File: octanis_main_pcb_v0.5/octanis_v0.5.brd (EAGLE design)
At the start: 69.2 x 41.9 mm, 78 parts, among them IC1 BME280, Q1 32.768kHz, Q2 32.768kHz, U3 DRV8836DSSR, U4 DRV8836DSSR, U5 DRV8836DSSR, U7 DRV8836DSSR

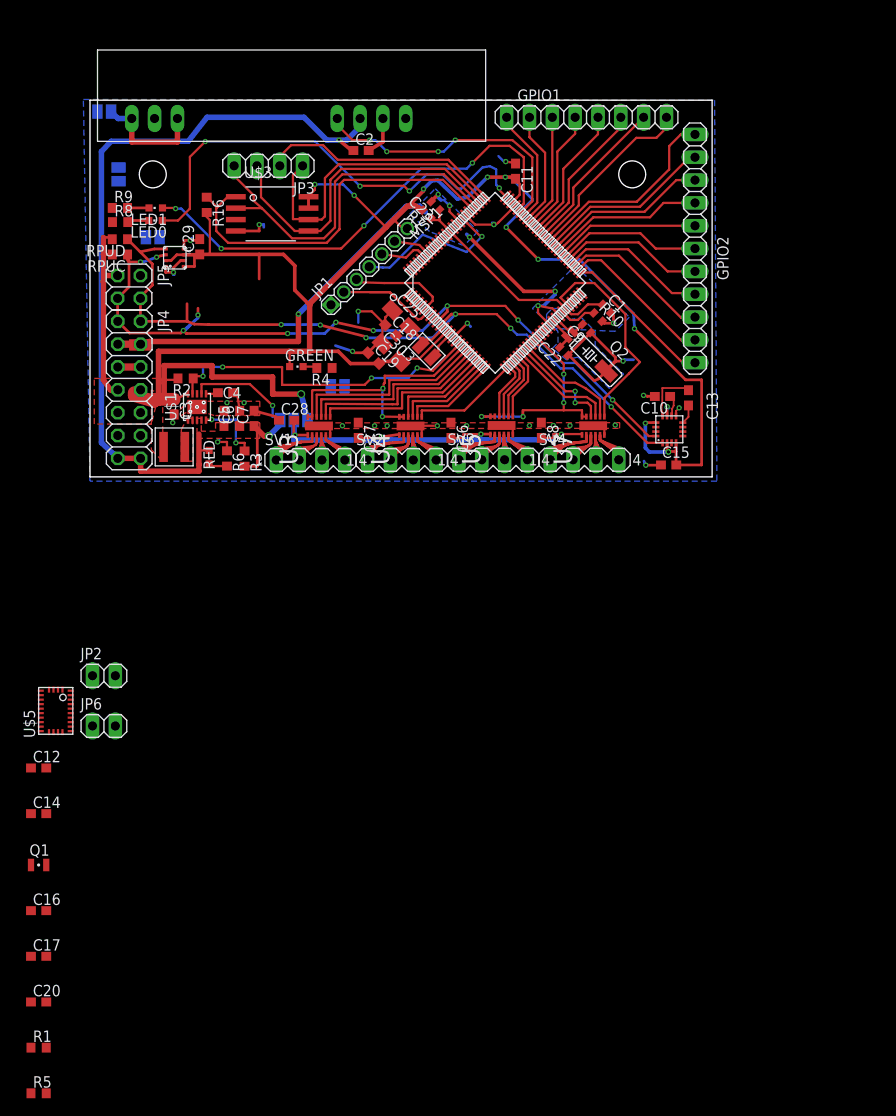
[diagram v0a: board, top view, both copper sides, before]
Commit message: rearranged GPIOs
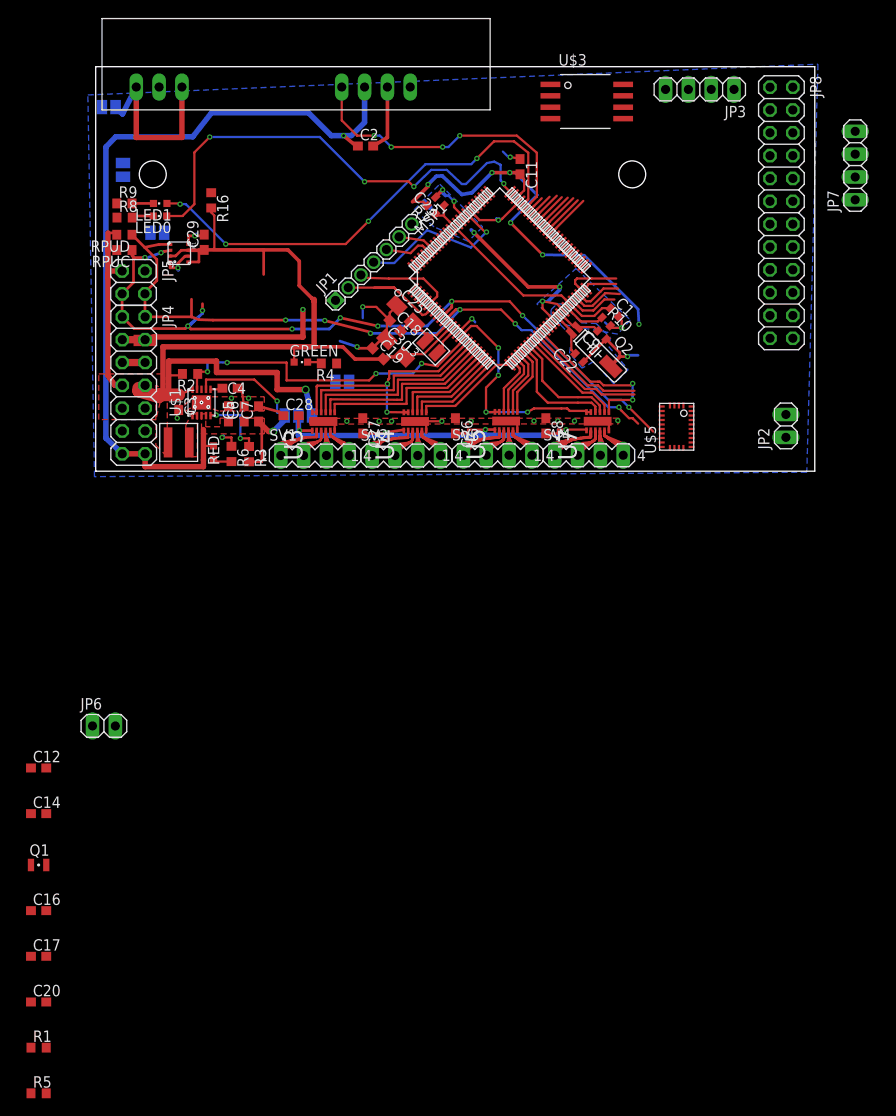
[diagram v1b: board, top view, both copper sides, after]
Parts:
- removed C10: 4.7u, rcl:C0603
- removed C13: 220n, rcl:C0603
- removed C15: 100n, rcl:C0603
- removed COMPASS: HMC5883L, HMC5883L:LPCC16
- removed GPIO1: A7:A0, pinhead:1X08
- removed GPIO2: A18:A8, pinhead:1X11
- added JP7: SPI, pinhead:1X04
- added JP8: (no value), pinhead:2X12
- moved JP2 80.8 mm to (76.8, 5.03), turned to 90 degrees
- moved U$5 76.0 mm to (64.6, 4.95)
- moved JP3 48.7 mm to (67.2, 42.5)
- moved U$3 37.2 mm to (53.5, 41.1)
- moved U$4 3.54 mm to (18.5, 42.7)
- moved C22 1.86 mm to (53.8, 12.6)
- moved C9 1.86 mm to (56.3, 15.2)
- moved R10 1.04 mm to (56.8, 16.6)
- moved C1 0.97 mm to (57.7, 17.7)
- moved C18 0.71 mm to (33.3, 16.2)
- moved C11 0.71 mm to (47.2, 33.9)
- moved C19 0.71 mm to (31.4, 13.1)
- moved C2 0.71 mm to (30.0, 36.2)
- moved C23 0.71 mm to (38.3, 30.0)
- moved C25 0.71 mm to (34.5, 17.4)
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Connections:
- removed net N$14: GPIO2.1, MSP1.61
- removed net N$15: GPIO2.2, MSP1.60
- removed net N$17: C10.1, COMPASS.10
- removed net N$20: GPIO2.3, MSP1.59
- removed net N$21: GPIO2.4, MSP1.58
- removed net N$22: GPIO2.5, MSP1.57
- removed net N$23: GPIO2.6, MSP1.56
- removed net N$25: C13.2, COMPASS.8
- removed net N$27: GPIO1.1, MSP1.69
- removed net N$28: GPIO1.2, MSP1.68
- removed net N$30: GPIO1.3, MSP1.67
- removed net N$32: C13.1, COMPASS.12
- removed net N$35: GPIO1.4, MSP1.66
- removed net N$36: GPIO1.5, MSP1.65
- removed net N$37: GPIO1.6, MSP1.64
- removed net N$38: GPIO1.8, MSP1.62
- removed net N$43: GPIO1.7, MSP1.63
- removed net P2.0/PM_UCA1STE: MSP1.16
- new net A0: JP8.1, MSP1.69
- new net A1: JP8.2, MSP1.68
- new net A10: JP8.11, MSP1.59
- new net A11: JP8.12, MSP1.58
- new net A12: JP8.13, MSP1.57
- new net A13: JP8.14, MSP1.56
- new net A2: JP8.3, MSP1.67
- new net A23: JP8.24, MSP1.46
- new net A3: JP8.4, MSP1.66
- new net A4: JP8.5, MSP1.65
- new net A5: JP8.6, MSP1.64
- new net A6: JP8.7, MSP1.63
- new net A7: JP8.8, MSP1.62
- new net A8: JP8.9, MSP1.61
- new net A9: JP8.10, MSP1.60
- net +3V3: no longer C15.2, COMPASS.13, COMPASS.2, COMPASS.4
- net A14: now also JP8.15; no longer GPIO2.7
- net A15: now also JP8.16; no longer GPIO2.8
- net A16: now also JP8.17; no longer GPIO2.9
- net A17: now also JP8.18; no longer GPIO2.10
- net A18: now also JP8.19; no longer GPIO2.11
- net A19: now also JP8.20
- net A20: now also JP8.21
- net A21: now also JP8.22
- net A22: now also JP8.23
- net GND: no longer C10.2, C15.1, COMPASS.11, COMPASS.9
- net M5678SLEEP: now also MSP1.16; no longer MSP1.36
- net M7IN1: now also MSP1.31; no longer MSP1.32
- net M7IN2: now also MSP1.32; no longer MSP1.31
- net M8IN2: now also MSP1.36; no longer MSP1.46
- net SCL: no longer COMPASS.1
- net SDA: no longer COMPASS.16
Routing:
- net +3V3: track 255.1 -> 188.5 mm, vias 12 -> 7
- net SPI_FLASH_CS: track 43.1 -> 0.00 mm
- net SPI_MISO: track 41.4 -> 0.00 mm
- net SPI_MOSI: track 36.5 -> 0.00 mm
- net SPI_SCK: track 34.1 -> 0.00 mm
- net SPI_EXTSLAVE_TE: track 26.7 -> 0.00 mm
- net N$14: track 22.6 -> 0.00 mm
- net N$38: track 20.2 -> 0.00 mm
- net N$15: track 19.8 -> 0.00 mm
- net N$20: track 18.5 -> 0.00 mm
- net N$43: track 17.6 -> 0.00 mm
- net N$21: track 17.3 -> 0.00 mm
- net A17: track 17.1 -> 0.00 mm
- net A18: track 16.8 -> 0.00 mm
- net A16: track 16.7 -> 0.00 mm
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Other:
- board size 69.2 x 41.9 mm -> 80 x 45 mm

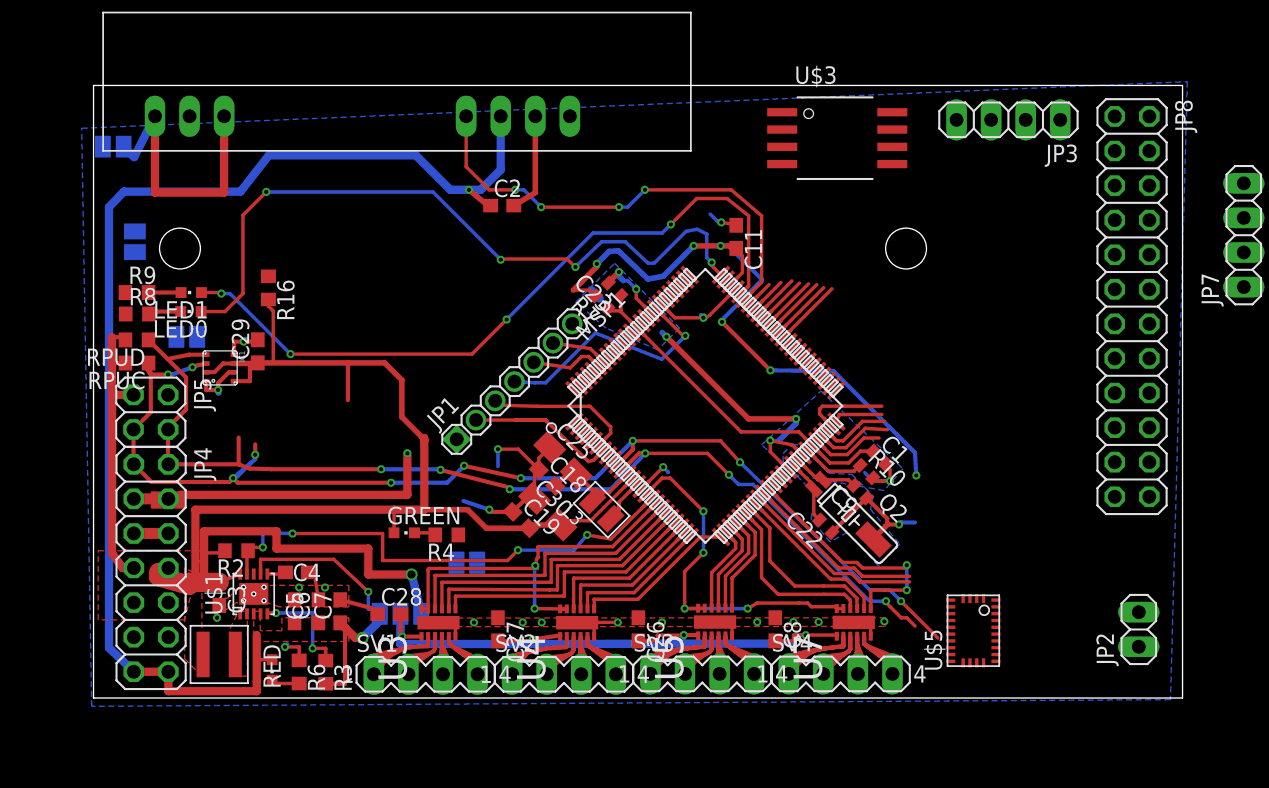
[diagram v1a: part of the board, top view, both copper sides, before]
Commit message: separated motor supply. added pull ups for sleep pin
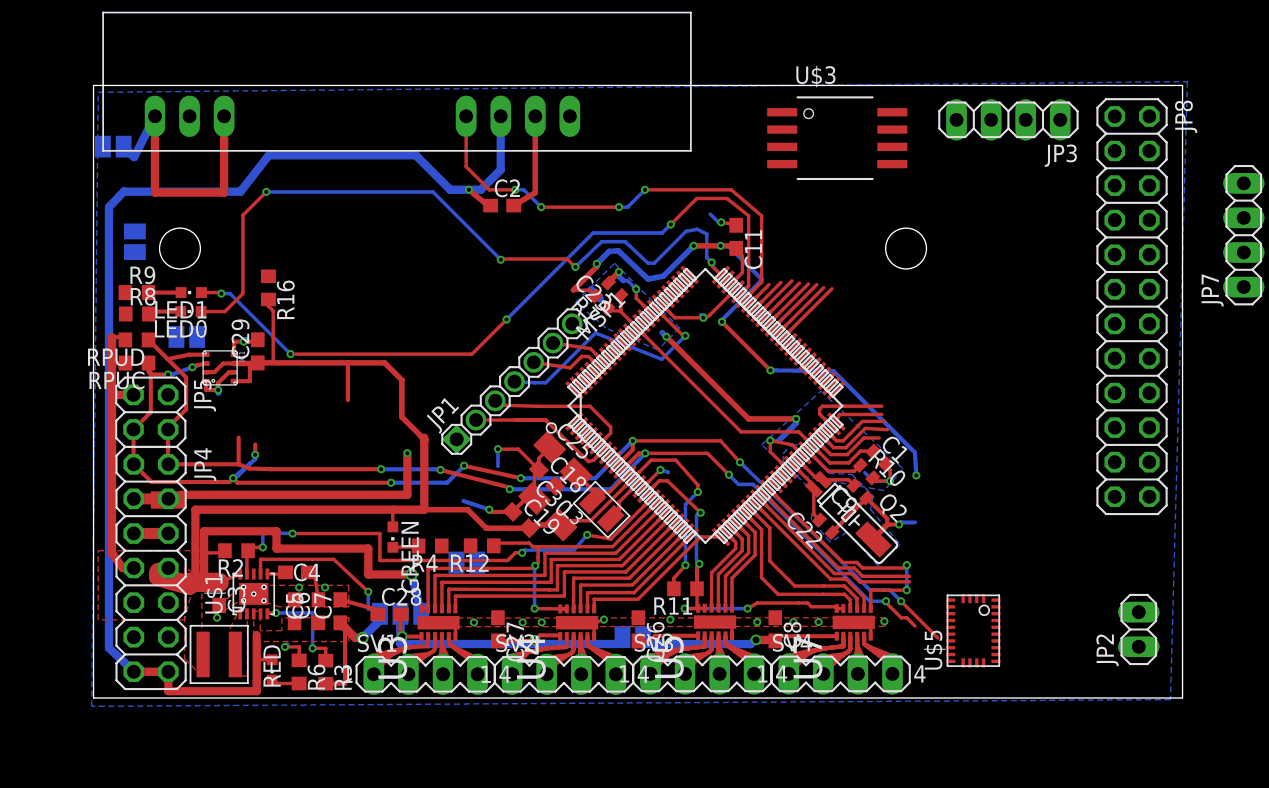
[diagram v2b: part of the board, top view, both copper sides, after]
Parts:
- added R11, R12: 10k, rcl:R0603
- added SJ6: (no value), jumper:SJ
- moved R4 1.47 mm to (24.7, 11.2)
- moved GREEN 0.90 mm to (22.0, 11.8), turned to 180 degrees
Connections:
- new net V_MOTOR2: C26.2, C8.2, SJ6.1, U5.1, U7.1
- net +3V3: now also R11.2, R12.2
- net M1234SLEEP: now also R12.1
- net M5678SLEEP: now also R11.1
- net V_MOTOR: now also SJ6.2; no longer C26.2, C8.2, U5.1, U7.1
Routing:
- net V_MOTOR: track 54.4 -> 30.7 mm, vias 4 -> 2
- net V_MOTOR2: track 0.00 -> 21.3 mm, vias 0 -> 2
- net +3V3: track 188.5 -> 202.7 mm, vias 7 -> 9
- net M1234SLEEP: track 28.6 -> 31.8 mm
- net GND: track 77.4 -> 76.2 mm
- net M5678SLEEP: track 26.8 -> 26.1 mm
- net N$4: track 1.59 -> 2.21 mm

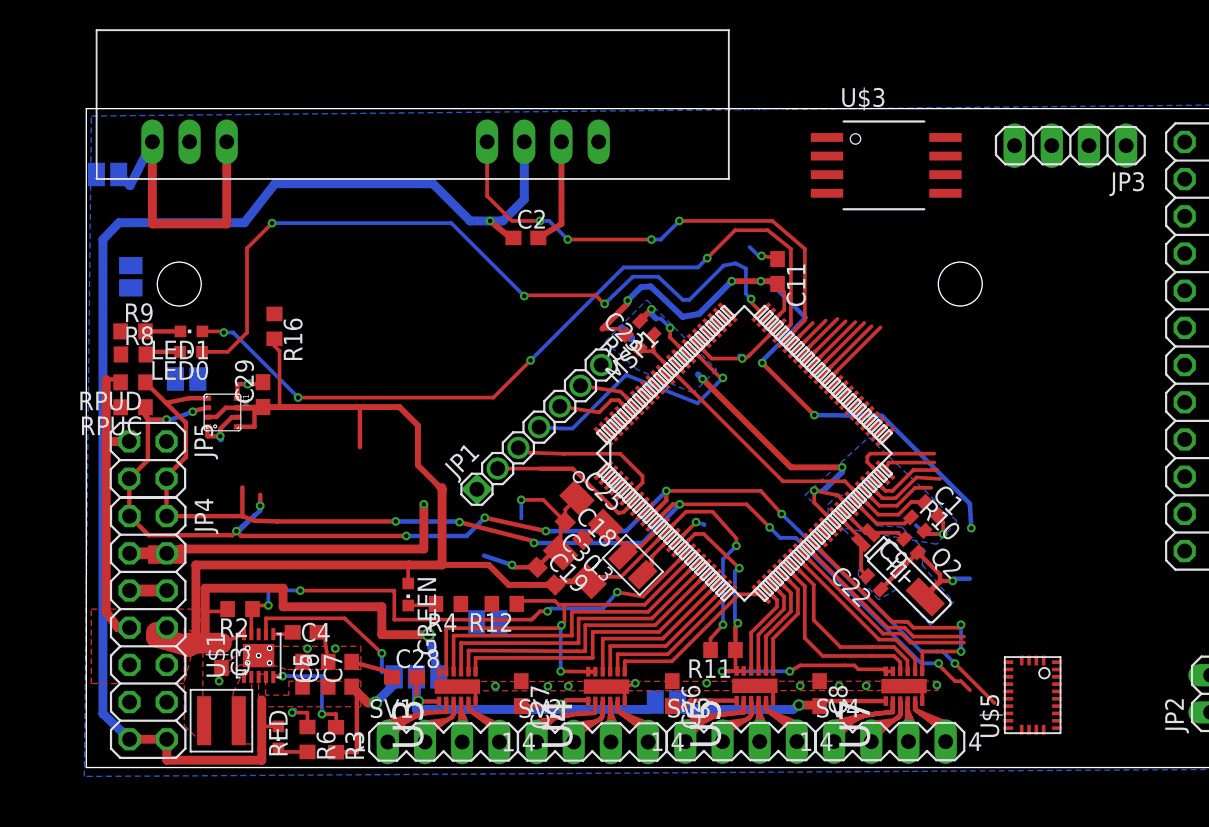
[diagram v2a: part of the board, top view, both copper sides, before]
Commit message: redesigned hx1 pins
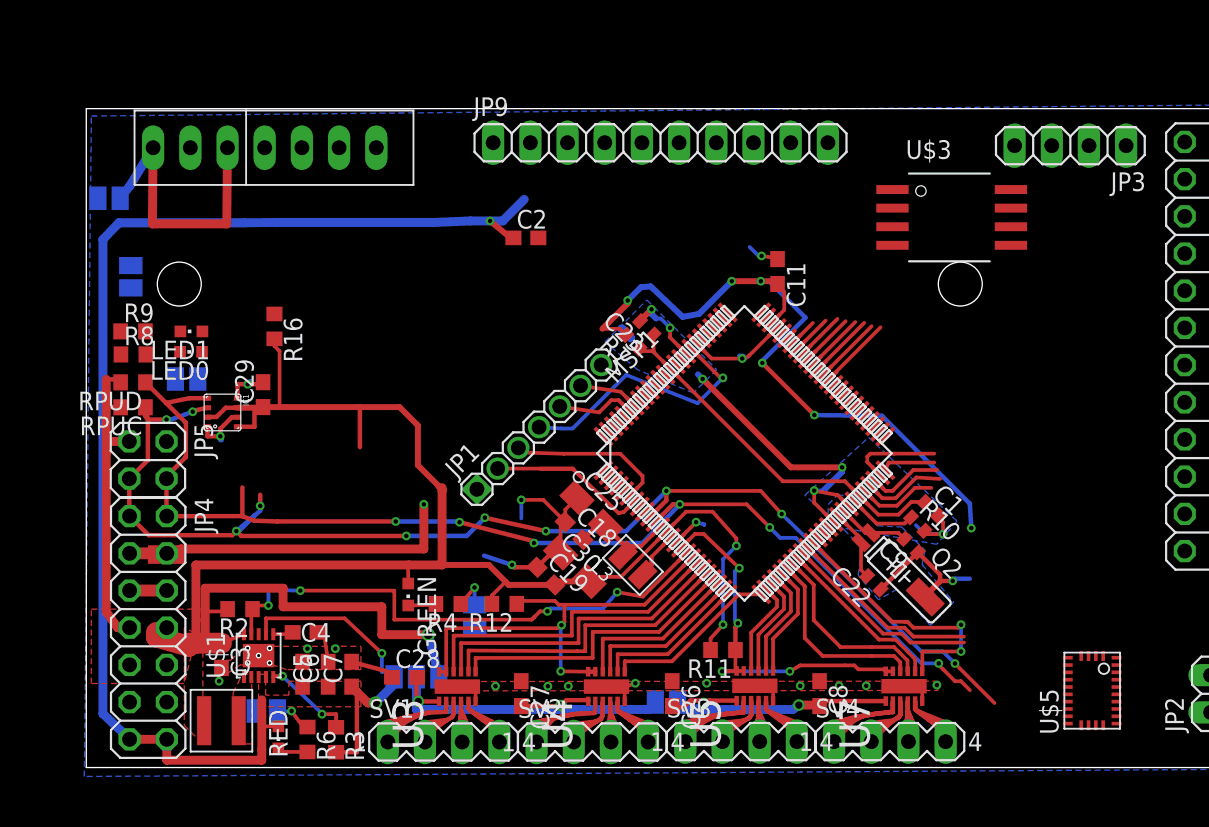
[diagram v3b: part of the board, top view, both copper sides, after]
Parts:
- added JP9: (no value), pinhead:1X10
- added SJ7: (no value), jumper:SJ
- U$4: value HX1 -> HX1EXTERNALMOUNT; device Octanis1:HX1 -> Octanis1:HX1_EXT
- moved U$4 13.9 mm to (4.56, 42.3)
- moved U$3 5.71 mm to (58.0, 37.6)
- moved U$5 4.08 mm to (68.7, 5.25)
- moved SJ2 1.63 mm to (1.55, 38.9)
- moved SJ3 0.99 mm to (26.5, 10.4), turned to 90 degrees
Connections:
- removed net P7.0/PM_SMCLK/PM_DMAE0: MSP1.88
- removed net P7.1/PM_C0OUT/PM_TA0CLK: MSP1.89
- removed net P7.2/PM_C1OUT/PM_TA1CLK: MSP1.90
- removed net P7.3/PM_TA0.0: MSP1.91
- new net N$14: R6.1, SJ7.2
- new net N$15: JP9.10, MSP1.88
- new net N$17: JP9.9, MSP1.89
- new net N$20: JP9.8, MSP1.90
- new net N$21: JP9.7, MSP1.91
- net GND: now also SJ7.1; no longer R6.1
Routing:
- net LED1: track 53.3 -> 0.00 mm, vias 4 -> 0
- net LED0: track 52.3 -> 0.00 mm, vias 4 -> 0
- net HX1_EN: track 34.5 -> 0.00 mm, vias 4 -> 0
- net GND: track 76.2 -> 66.4 mm, vias 21 -> 20
- net +5V: track 113.3 -> 107.0 mm
- net N$14: track 0.00 -> 2.83 mm, vias 0 -> 1
- net N$26: track 0.00 -> 2.64 mm, vias 0 -> 1
- net N$5: track 2.41 -> 0.00 mm
- net N$6: track 2.39 -> 0.00 mm
- net +3V3: track 202.7 -> 204.6 mm
- net N$2: track 7.81 -> 6.28 mm
- net RFGND: track 20.8 -> 19.6 mm

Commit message: assigned all GPIO
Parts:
- removed JP2: (no value), pinhead:1X02
- removed SJ4, SJ5: (no value), jumper:SJ
- added C10: 10u, rcl:A/3216-18R
- added JP10: (no value), pinhead:2X10
- JP3: value SPI -> (none); device pinhead:1X04 -> pinhead:2X02
- JP6: device pinhead:1X02 -> pinhead:2X02
- JP9: device pinhead:1X10 -> pinhead:2X02
- moved R5 114.1 mm to (76.2, 9.53)
- moved R1 107.3 mm to (69.8, 11.4), turned to 270 degrees
- moved C20 104.1 mm to (76.2, 4.45)
- moved C16 96.4 mm to (75.6, 1.91)
- moved C14 94.1 mm to (76.2, 6.99)
- moved C17 93.0 mm to (67.9, 1.91), turned to 180 degrees
- moved Q1 90.8 mm to (71.8, 2.54)
- moved C12 90.4 mm to (72.4, 11.4), turned to 270 degrees
- moved JP6 73.4 mm to (64.1, 8.89), turned to 90 degrees
- moved JP3 64.2 mm to (3.81, 32.4), turned to 90 degrees
- moved R16 54.5 mm to (66.2, 41.6), turned to 90 degrees
- moved SJ2 34.0 mm to (1.28, 4.87), turned to 90 degrees
- moved C2 17.4 mm to (12.8, 38.0)
- moved LED0 15.9 mm to (22.6, 32.3)
- moved R8 15.5 mm to (18.2, 32.2)
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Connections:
- removed net N$24: U$4.TXD
- removed net N$29: R8.1, SJ4.2
- removed net N$31: R9.1, SJ5.2
- removed net P1.0/UCA0STE: MSP1.4
- removed net P1.1/UCA0CLK: MSP1.5
- removed net P1.4/UCB0STE: MSP1.8
- removed net P1.5/UCB0CLK: MSP1.9
- removed net P10.0/UCB3STE: MSP1.100
- removed net P10.1/UCB3CLK: MSP1.1
- removed net P10.2/UCB3SIMO/UCB3SDA: MSP1.2
- removed net P10.3UCB3SOMI/UCB3SCL: MSP1.3
- removed net P3.5/PM_UCB2CLK: MSP1.37
- removed net P6.7/TA2.4/UCB3SOMI/UCB3SCL/C1.0: MSP1.81
- removed net P9.2/TA3.3: MSP1.74
- removed net P9.4/UCA3STE: MSP1.96
- removed net P9.5/UCA3CLK: MSP1.97
- removed net PJ.2/HFXOUT: MSP1.85
- removed net PJ.3/HFXIN: MSP1.86
- removed net PJ.4/TDI/ADC14CLK: MSP1.92
- removed net PJ.5/TDO/SWO: MSP1.93
- new net HX1_DATA: MSP1.8, U$4.TXD
- new net P1.0: JP10.20, MSP1.4
- new net P1.1: JP10.19, MSP1.5
- new net P10.2: JP10.17, MSP1.2
- new net P10.3: JP10.18, MSP1.3
- new net P5.6: JP10.7, MSP1.70
- new net P5.7: JP10.5, MSP1.71
- new net P6.6: JP10.10, MSP1.80
- new net P6.7: JP10.9, MSP1.81
- new net P9.2: JP10.3, MSP1.74
- new net P9.3: JP10.1, MSP1.75
- new net P9.4: JP10.15, MSP1.96
- new net P9.5: JP10.16, MSP1.97
- new net PJ.2: JP10.13, MSP1.85
- new net PJ.3: JP10.14, MSP1.86
- new net PJ.4: JP10.11, MSP1.92
- new net PJ.5: JP10.12, MSP1.93
- net +3V3: now also JP6.1
- net +5V: now also C10.+, JP3.2
- net GND: now also JP3.4, JP6.3, R8.1, R9.1; no longer C2.2, SJ4.1, SJ5.1, U$4.0V
- net HX1_EN: now also MSP1.9; no longer MSP1.70
- net LED0: now also MSP1.100; no longer MSP1.75
- net LED1: now also MSP1.1; no longer MSP1.71
- net N$15: now also JP10.2; no longer JP9.10
- net N$17: now also JP10.4; no longer JP9.9
- net N$19: now also Q1.2
- net N$20: now also JP10.6; no longer JP9.8
- net N$21: now also JP10.8; no longer JP9.7
- net RFGND: now also C10.-, C2.2, U$4.0V
- net RX2: now also JP6.2; no longer JP2.2
- net RX3: now also JP3.1; no longer JP6.1
- net SCL: now also JP4.1, JP5.3; no longer JP4.2, JP5.4
- net SDA: now also JP4.2, JP5.4; no longer JP4.1, JP5.3
- net SPI_EXTSLAVE_TE: now also JP9.1; no longer JP3.2
- net SPI_FLASH_CS: now also MSP1.37; no longer MSP1.80
- net SPI_MISO: now also JP9.2; no longer JP3.4
- net SPI_MOSI: now also JP9.4; no longer JP3.3
- net SPI_SCK: now also JP9.3; no longer JP3.1
- net TX2: now also JP6.4; no longer JP2.1
- net TX3: now also JP3.3; no longer JP6.2
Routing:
- net HX1_EN: track 0.00 -> 67.8 mm, vias 0 -> 6
- net HX1_DATA: track 0.00 -> 58.7 mm, vias 0 -> 6
- net +3V3: track 204.6 -> 260.1 mm, vias 9 -> 11
- net RX3: track 0.00 -> 42.1 mm
- net TX3: track 0.00 -> 36.0 mm
- net SPI_FLASH_CS: track 0.00 -> 33.6 mm, vias 0 -> 4
- net RFGND: track 19.6 -> 45.8 mm
- net P1.1: track 0.00 -> 17.1 mm
- net LED1: track 0.00 -> 17.0 mm
- net LED0: track 0.00 -> 17.0 mm
- net N$76: track 4.11 -> 21.0 mm, vias 0 -> 2
- net P10.2: track 0.00 -> 16.3 mm, vias 0 -> 1
- net AGND: track 51.8 -> 35.9 mm, vias 7 -> 5
- net N$77: track 5.42 -> 21.2 mm, vias 0 -> 2
- net PJ.4: track 0.00 -> 14.8 mm
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- added copper zone on layer 16, net RFGND
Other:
- board text added: "5V |GND| 3.3V | GND | SCL | 3.3V"
- board text added: "SDA | GND"
- board text removed: "5V |GND| 3.3V | GND | SDA | 3.3V"
- board text removed: "SCL | GND"
